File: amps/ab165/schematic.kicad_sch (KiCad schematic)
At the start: 105 parts

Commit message: AB165: input leaks, treble cap, OT centre tap, bias bridge (V1 audit)
Read against the cited D-FE schematic (el34world, 7087x4274, native):

- Input leaks: each channel's 1M hangs from jack 1's tip, jack side of
  its lower 68k (Bass crop 140,950,1300,2150; Normal 140,2700,1300,3900).
  The sheet had both on the grid bus. R1b/R1n declared series_bridge
  (the AB763 idiom); the board already mounts both at the jacks.
- CTB, the Bass channel treble cap, is lettered 330 PF, not 390 (crop
  1400,995,1500,1045: two left-side notches like the label's own 3, no
  closed left bowl). BOM, sheet, notes, meta desc and board caption.
- OT centre tap: D-FE takes it from the standby node, on the reservoir
  side of the choke; the screens, the first 20-525 and the 1k dropper
  hang on the choke output (crop 5300,2050,7000,3800). Both surfaces
  had it on the choke output. Sheet: new B+0 node, TR2.1/TR2.2 anchored
  to BP1. Board: TR3.red -> TR2.plate, both choke leads anchored to BP1,
  the stale not_on_board[TR2] dropped.
- Bias: one filter capacitor, not two (CB2 removed). The 10K-L sits
  across the diode node and a 15K foot, a 10K from each end meets at one
  junction; V5's 220k returns to the wiper (-45V), V6's to that
  junction (crop 4300,2050,5600,3000). Sheet redrawn; roles and the
  board caption corrected.
- BOM note: two jacks per channel with contacts; one bias capacitor.

No DC node moves: netlist.cir and voltages.yaml are untouched.

Co-Authored-By: Claude Opus 5.5 <noreply@anthropic.com>
Claude-Session: https://claude.ai/code/session_01KBMfdh37HmCL2iWcBiL5J1
Signed-off-by: AnalogMaker <theanalogmaker@gmail.com>
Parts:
- removed C10: 70u, symbol cx:C
- removed C15: 8u, symbol cx:C
- removed CB2: elec, symbol cx:C
- removed CBN, CDEEP: .1u, symbol cx:C
- removed CBN2: .047u, symbol cx:C
- removed CMIX: .01u, symbol cx:C
- removed CTN: 250p, symbol cx:C
- removed D1: Si x3, symbol cx:DIODE_SS
- removed R2n: 68k, symbol cx:R
- removed RBIAS: 470 1W, symbol cx:R
- removed RLM, RLN1, RLN2: 100k, symbol cx:R
- removed RLPA: 100k 5%, symbol cx:R
- removed RTAIL: 470, symbol cx:R
- removed TR1: 125P7D, symbol cx:PT
- added CBRN: 120p, symbol cx:C
- added D2: Si x3, symbol cx:DIODE_SS
- added DBIAS: Si, symbol cx:DIODE_SS
- added RBAL1: 220k 1W, symbol cx:R
- added RGM: 470k, symbol cx:R
- added RGN1: 1M, symbol cx:R
- added RKM, RKN1, RKN2: 1.5k, symbol cx:R
- added RLPB: 100k 5%, symbol cx:R
- added RT2: 22k, symbol cx:R
- added SWAC: AC, symbol cx:SWITCH
- added SWDEEP: DEEP, symbol cx:SWITCH
- added VRBAL: 10k-L bal, symbol cx:POT
- added VRBN: 250k bass, symbol cx:POT
- added VRTN: 250k treb, symbol cx:POT
- C10: renamed from RBAL1; value 220k 1W -> 70u; symbol cx:R -> cx:C
- C15: renamed from RD3; value 27k 1W -> 8u; symbol cx:R -> cx:C
- CB1: renamed from VRBAL; value 10k-L bal -> elec; symbol cx:POT -> cx:C
- CBN: renamed from VRBN; value 250k bass -> .1u; symbol cx:POT -> cx:C
- CBN2: renamed from RSLN; value 6.8k -> .047u; symbol cx:R -> cx:C
- CDEEP: renamed from SWDEEP; value DEEP -> .1u; symbol cx:SWITCH -> cx:C
- CMIX: renamed from RGM; value 470k -> .01u; symbol cx:R -> cx:C
- CTB: value 390p -> 330p
- CTN: renamed from VRTN; value 250k treb -> 250p; symbol cx:POT -> cx:C
- R2n: renamed from RGN1; value 1M -> 68k
- RBIAS: renamed from CB1; value elec -> 470 1W; symbol cx:C -> cx:R
- RD3: renamed from DBIAS; value Si -> 27k 1W; symbol cx:DIODE_SS -> cx:R
- RLM: renamed from RKM; value 1.5k -> 100k
- RLN1: renamed from RKN1; value 1.5k -> 100k
- RLN2: renamed from RKN2; value 1.5k -> 100k
- RSLN: renamed from VRVN; value 1M vol -> 6.8k; symbol cx:POT -> cx:R
- RTAIL: renamed from RT2; value 22k -> 470
- TR1: renamed from SWAC; value AC -> 125P7D; symbol cx:SWITCH -> cx:PT
- VRVN: renamed from CBRN; value 120p -> 1M vol; symbol cx:C -> cx:POT
- renumbered D2 to D1, RLPB to RLPA
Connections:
- net -45V A: now also VRBAL.2 (W); no longer RBB1.1
- net -45V B: now also RBB1.1
- net B+1: no longer TR3.2 (CT)
- net B+2: now also RLPB.1
- net B+3: now also RD3.1, RLM.1, RLN2.1; no longer C15.1
- net B+4: now also C15.1, RD3.2, RLN1.1; no longer C15.2
- net BASS 1: now also RGB1.2
- net GND: now also C15.2, CB1.2, RGB1.1, RSLN.2, TR1.4 (HT_CT), VRVN.3, RGM.2, RGN1.1, RKM.2, RKN1.2, RKN2.2, RT2.2, SWDEEP.2; no longer CBN2.2, CDEEP.2, CMIX.2, R2n.2, RBIAS.2, RGB1.2, RLM.2, RLN1.2, RLN2.2, RSLN.3, RTAIL.2
- net MAINS N: now also TR1.2 (PRI_2)
- net MIX: now also CMIX.1
- net NORM 1: now also RGN1.2
- net NORM 2: now also R2n.1
- net at D1.1 (A): now also TR1.3 (HT_A)
- net at RGPA.2, RGPB.1, RTAIL.1: now also RT2.1
- net at CBB.1, CBB2.1: now also CDEEP.1
- net at F1.2: now also SWAC.1; no longer TR1.1
- net at CPIA.1, RFBM.2, V3B.1 (P): now also RLM.2
- net at RSN.1, V2A.1 (P): now also RLN1.2
- net at CKN2.1, V2B.3 (K): now also RKN2.1; no longer RLN2.1
- net at C10.1, D1.2 (K), SWSTBY.1: now also D2.2 (K), RBAL1.1
- net B+0: now reaches SWSTBY.2, TR2.1
- net B+0: now also TR3.2 (CT)
- net at C10.2, C11.1, RBAL2.1: now also RBAL1.2
- net at CBN2.1: now also CBN.1; no longer CBN.3
- net at CKN1.1, V2A.3 (K): now also RKN1.1; no longer RLN1.1
- net at RMXN.1, V2B.1 (P): now also RLN2.2
- net at SWBRT.2, V2B.2 (G): now also VRVN.2 (W); no longer RSLN.2 (W)
- net at R1n.2, V2A.2 (G): now also R2n.2; no longer R2n.1
- net at C1.1, RBSA.1, V4A.1 (P): now also RLPA.2
- net at CKM.1, V3B.3 (K): now also RKM.1; no longer RLM.1
- net at R1b.2, R2b.2, V1A.2 (G): no longer RGB1.1
- net at V4A.3 (K), V4B.3 (K): now also RTAIL.2
- net at C2.1, RBSB.1, V4B.1 (P): now also RLPB.2; no longer RLPA.2
- net at SWBRT.1: now also CBRN.2; no longer VRVN.2
- net at V3B.2 (G): now also CMIX.2, RGM.1; no longer CMIX.1
- new net: CDEEP.2, SWDEEP.1
- new net: SWAC.2, TR1.1 (PRI_1)
- new net: D2.1 (A), RBIAS.1, TR1.5 (HT_B)
- new net: RBB1.2, RBB3.1, VRBAL.3
- new net: CBRN.1, VRTN.2 (W), VRVN.1
- new net: CBN.2, VRBN.1, VRBN.2 (W), VRTN.3
- new net: CB1.1, DBIAS.1 (A), RBB2.2, VRBAL.1
- new net: DBIAS.2 (K), RBIAS.2
- new net: CTN.2, VRTN.1
- new net: CBN2.2, RSLN.1, VRBN.3
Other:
- note added: "Bias supply — one HT lead through 470 Ω · 1 W and a silicon diode, one filter can; the 10 kΩ-L hum-balance pot and its two 10 kΩ legs form a bridge: V5 returns to the wiper (-45 V), V6 to the legs' junction"
- note removed: "Bias supply — one HT leg through 470 Ω · 1 W and a silicon diode; the 10 kΩ-L balance control gives each output tube its own 10 kΩ leg"
- moved on the sheet: D1, R1b, R2n, RLM, RLN1, RLN2, RLPA, RTAIL

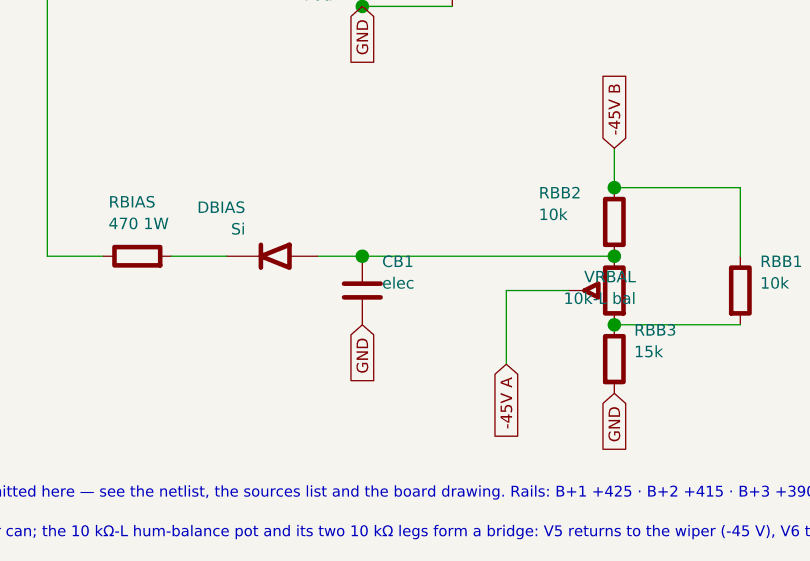
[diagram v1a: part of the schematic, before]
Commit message: AB165: bias filter 50 µF · 50 V from the layout page; layout cited as a source (V1 audit)
The D-FE layout page (el34world Fender_bassman_ab165_layout.pdf, sha1
fb28fd70..., one 2148x1578 page at 200 ppi), which layout.yaml already
cited, is added to meta.yaml sources. Its bias board (crop
170,400,920,680) carries exactly one electrolytic, lettered '50 | 50'
with + and -, so CB1 is 50 µF · 50 V; the schematic draws that one
capacitor and prints no value. This settles F5 (one can) on both pages.
The same crop draws the 15K and the two 10K legs at the 10K-L as the
schematic does (F4). The Bass channel's treble cap is lettered 330 on
the board (crop 1722,825,1752,885), agreeing with F2. CB1 is off the
eyelet board (not_on_board), so no board `plus:` changes; its + goes to
ground on both pages. No DC node moves.

Co-Authored-By: Claude Opus 5.5 <noreply@anthropic.com>
Claude-Session: https://claude.ai/code/session_01KBMfdh37HmCL2iWcBiL5J1
Signed-off-by: AnalogMaker <theanalogmaker@gmail.com>
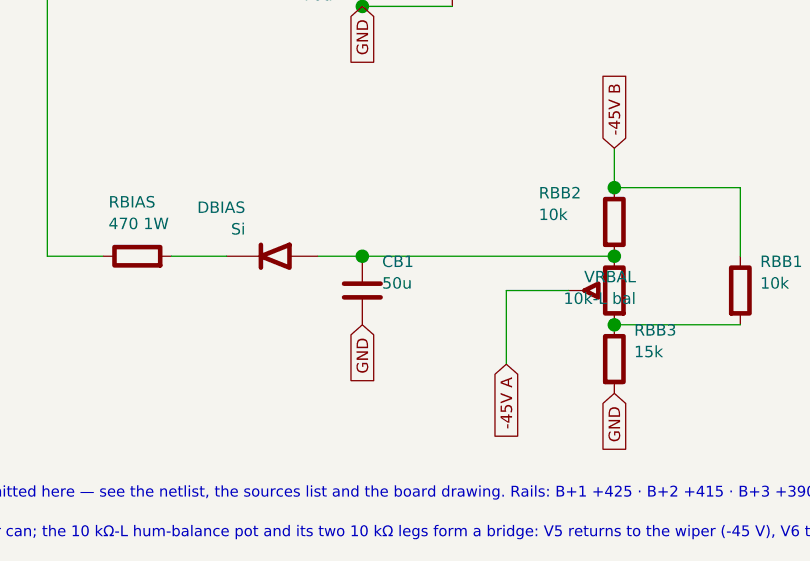
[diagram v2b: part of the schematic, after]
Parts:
- CB1: value elec -> 50u
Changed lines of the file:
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@@
     (in_bom yes) (on_board yes)
     (property "Reference" "CB1" (at 118.672 242.43 0) (effects (font (size 1.27 1.27)) (justify left)))
-    (property "Value" "elec" (at 118.672 244.83 0) (effects (font (size 1.27 1.27)) (justify left))))
+    (property "Value" "50u" (at 118.672 244.83 0) (effects (font (size 1.27 1.27)) (justify left))))
   (global_label "GND" (shape input) (at 116.472 249.44 270)
     (effects (font (size 1.27 1.27)) (justify right)))
